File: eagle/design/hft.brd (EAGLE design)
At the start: 59.7 x 54.3 mm, 37 parts

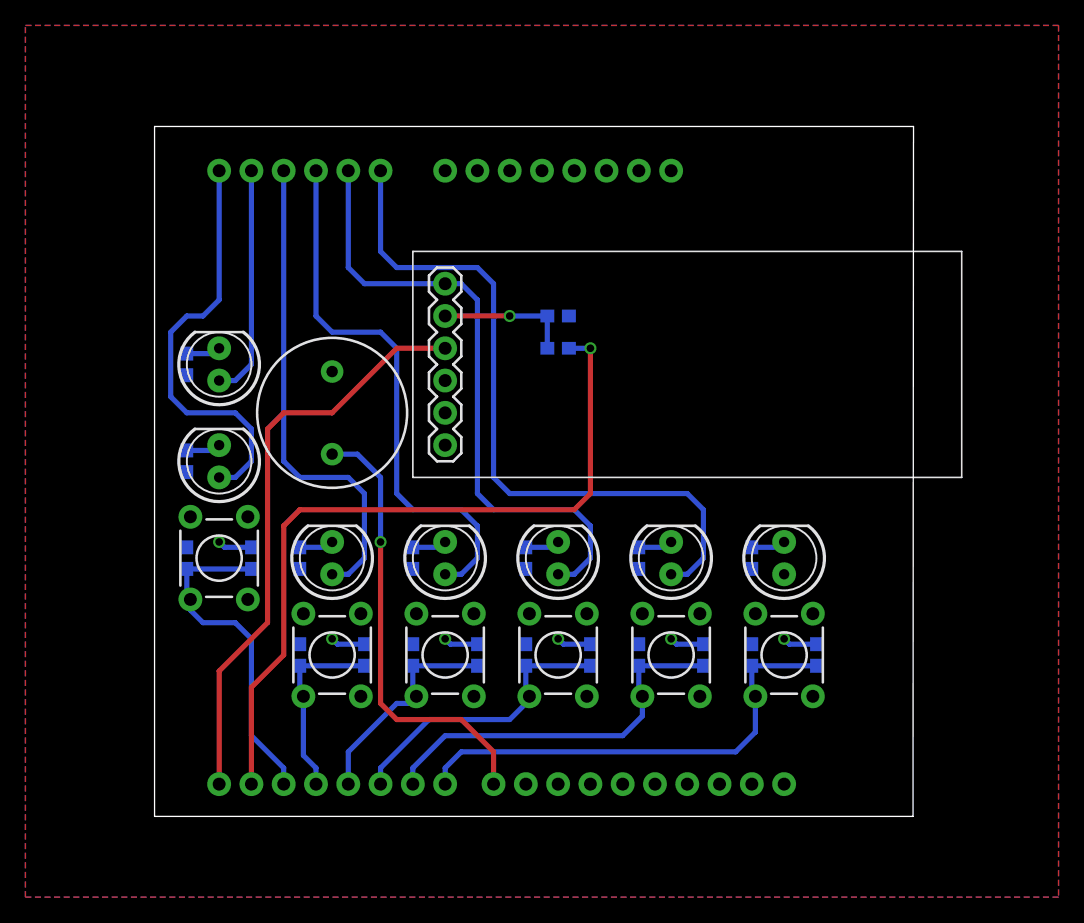
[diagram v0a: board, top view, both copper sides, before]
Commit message: Re-organize directory and update .gitignore.
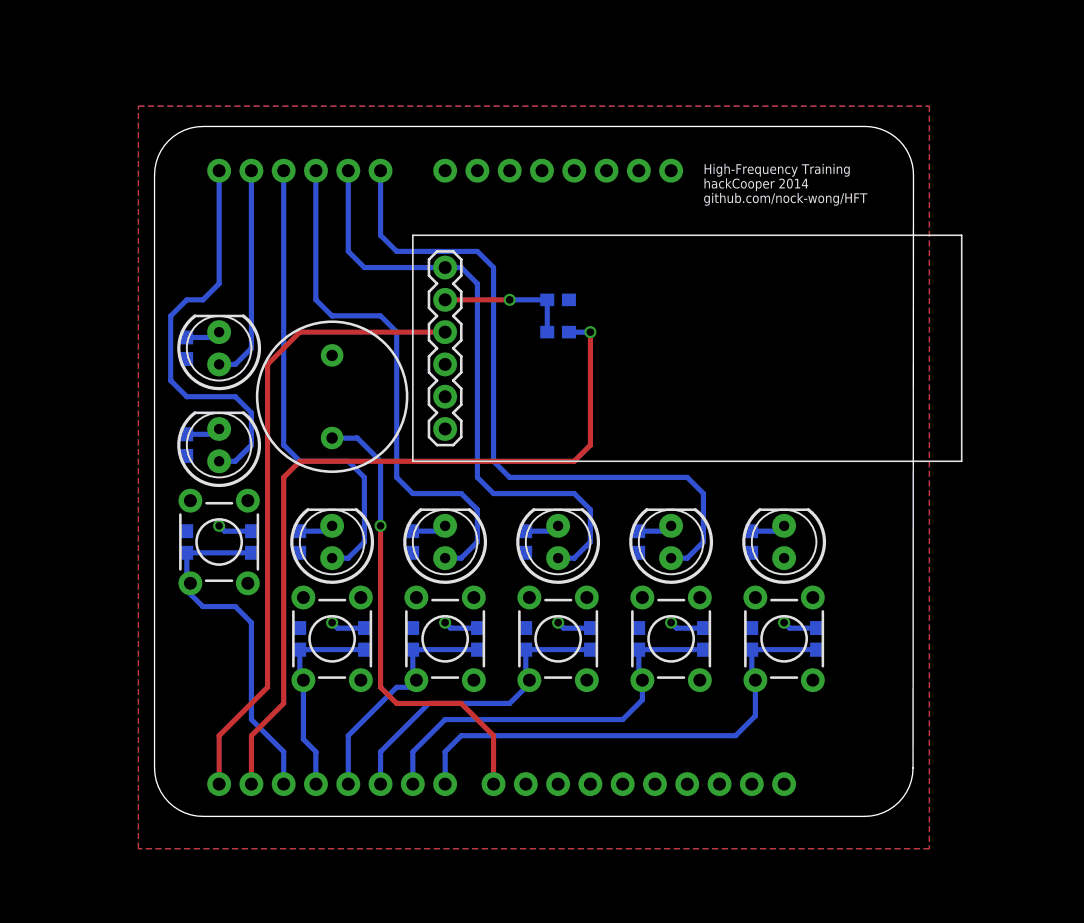
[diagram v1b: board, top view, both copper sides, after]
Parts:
- moved R14 1.27 mm to (31.8, 38.1)
- moved R15 1.27 mm to (31.8, 40.6)
- moved SG1 1.27 mm to (14.0, 33.0)
- moved C2 1.27 mm to (11.4, 14.0)
- moved C3 1.27 mm to (20.3, 14.0)
- moved C4 1.27 mm to (29.2, 14.0)
- moved C5 1.27 mm to (38.1, 14.0)
- moved C6 1.27 mm to (47.0, 14.0)
- moved R10 1.27 mm to (43.2, 14.0)
- moved R12 1.27 mm to (52.1, 14.0)
- moved R4 1.27 mm to (16.5, 14.0)
- moved R6 1.27 mm to (25.4, 14.0)
- moved R8 1.27 mm to (34.3, 14.0)
- moved S2 1.27 mm to (14.0, 14.0)
- moved S3 1.27 mm to (22.9, 14.0)
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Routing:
- net ARD-RX: track 46.1 -> 49.6 mm
- net ARD-TX: track 59.7 -> 60.9 mm
- net SPK: track 35.4 -> 36.6 mm
- net LED3: track 56.0 -> 54.7 mm
- net LED2: track 49.6 -> 48.4 mm
- net LED1: track 43.3 -> 42.0 mm
- net LED6: track 33.1 -> 31.8 mm
- net LED5: track 18.3 -> 17.0 mm
- net B4: track 30.2 -> 31.4 mm
- net B1: track 14.9 -> 16.2 mm
- net LED0: track 38.4 -> 37.1 mm
- net B5: track 37.3 -> 38.5 mm
- net B3: track 23.1 -> 24.3 mm
- net B2: track 17.3 -> 18.6 mm
- net B0: track 26.7 -> 27.9 mm
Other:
- outline, holes or cut-outs redrawn
- board text added: "High-Frequency Training hackCooper 2014 github.com/nock-wong/HFT"
